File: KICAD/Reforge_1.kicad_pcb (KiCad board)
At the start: 2 copper layers, 57.9 x 76 mm, 94 parts, among them J1 USB_C_Receptacle_USB2.0_16P, J10 Conn_01x14_Pin, J11 Conn_01x12_Pin, J12 Conn_01x12_Pin, J14 Conn_01x12_Pin, J15 Conn_01x12_Pin, J3 Conn_01x02, J8 Conn_01x12_Pin, J9 Conn_01x14_Pin, Q1 SS8050, Q2 SS8050, SW1 SW_Push, SW2 SW_Push, U11 SN74LVC2G125DCUR, U2 CP2102N-Axx-xQFN28, U3 ICE40UP5K-SG48ITR, U4 AP2112K-1.2, U5 ESP32-WROOM-32D, U6 AMS1117-3.3, U8 W25Q32JVSS, Y1 SG-210STF

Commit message: Update schematic and PCB
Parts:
- removed C26, C27, C28: DNI, Capacitor_SMD:C_0805_2012Metric
- removed the G*** at (130.1, 58.2)
- removed R7, R8: 0R(5%), Resistor_SMD:R_0805_2012Metric_Pad1.20x1.40mm_HandSolder
- removed TP1, TP2, TP8: TestPoint, TestPoint:TestPoint_Pad_D1.0mm
- removed VBUS1: TestPoint, LED_SMD:LED_RGB_Wuerth-PLCC4_3.2x2.8mm_150141M173100
- added G***: LOGO, LOGO, F.Cu at (122.5, 87.4)
- added G***: LOGO, LOGO, B.Cu at (129.5, 60.2)
- added G***: LOGO, LOGO, B.Cu at (158.5, 66.4)
- C16, Q1, R10, R19, R4, R9, U2, U8: moved to F.Cu
- R20: footprint Resistor_SMD:R_0402_1005Metric -> Resistor_SMD:R_0805_2012Metric_Pad1.20x1.40mm_HandSolder
- SJ31, SJ34: moved to B.Cu
- moved C8 64.0 mm to (159.4, 60.4), turned to 0 degrees
- moved R1 62.3 mm to (117.0, 55.8)
- moved C9 61.5 mm to (159.4, 62.5), turned to 0 degrees
- moved SJ26 38.0 mm to (122.9, 107.0), turned to 0 degrees
- moved C16 37.9 mm to (128.7, 114.4), turned to -90 degrees
- moved C24 36.2 mm to (142.2, 108.3), turned to -90 degrees
- moved C2 33.9 mm to (116.9, 49.4), turned to 0 degrees
- moved SJ19 32.8 mm to (122.8, 99.5), turned to 0 degrees
- moved C1 31.1 mm to (116.8, 51.5), turned to 180 degrees
- moved C13 30.0 mm to (128.9, 99.2), turned to 90 degrees
- moved C14 29.6 mm to (138.4, 105.5)
- moved C12 29.0 mm to (126.8, 99.2), turned to 90 degrees
- moved SJ31 28.2 mm to (127.7, 99.3), turned to -90 degrees
- moved C5 27.9 mm to (131.6, 79.2), turned to -90 degrees
- moved C7 25.1 mm to (133.3, 84.6), turned to 180 degrees
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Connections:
- J10 pad 4: /TXD0 -> /RXD
- Q2 pad 2: /IO0 -> /~{DTR}
- Q2 pad 3: /~{DTR} -> /IO0
- U2 pad 26: /TXD -> /RXD0
- U5 pad 35: /TXD0 -> /RXD
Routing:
- net /VDD33: track 275.1 -> 0.00 mm, vias 12 -> 0
- net /EN: track 132.6 -> 0.00 mm, vias 2 -> 0
- net /VCCIO_2: track 72.4 -> 0.00 mm, vias 3 -> 0
- net /FT_SCK: track 67.6 -> 0.00 mm
- net /VCCIO_0: track 51.8 -> 0.00 mm, vias 6 -> 0
- net /CLK: track 48.1 -> 0.00 mm, vias 3 -> 0
- net /CDONE: track 43.8 -> 0.00 mm, vias 3 -> 0
- net /FT_SSn: track 43.0 -> 0.00 mm, vias 5 -> 0
- net /+1.2V_CORE: track 42.3 -> 0.00 mm
- net /USB_DP: track 41.2 -> 0.00 mm, vias 4 -> 0
- net /IOB_25B_G3: track 41.1 -> 0.00 mm, vias 2 -> 0
- net /EXT_5V: track 39.4 -> 0.00 mm
- net /IO0: track 36.2 -> 0.00 mm, vias 4 -> 0
- net /FPGA_SO: track 33.8 -> 0.00 mm
- net /FPGA_SI: track 31.8 -> 0.00 mm, vias 2 -> 0
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- added copper zone on F.Cu, net /VDD33
- removed copper zone on F.Cu, net GND
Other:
- board size 57.9 x 76 mm -> 66.5 x 80.4 mm
- board text added: "AMRIT"
- board text added: "SURAJ"

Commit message: UPDATED PCB
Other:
- board text added: "BOOT"
- board text added: "EN"
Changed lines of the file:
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@@
 		(tags "resistor handsolder")
 		(property "Reference" "R9"
-			(at -0.06 -1.71 90)
+			(at -1.85 -1.71 180)
 			(layer "F.SilkS")
 			(effects
 				(font
-					(size 1 1)
-					(thickness 0.15)
+					(size 0.5 0.5)
+					(thickness 0.125)
 				)
 			)
@@
 			(effects
 				(font
-					(size 1 1)
-					(thickness 0.15)
+					(size 0.5 0.5)
+					(thickness 0.125)
 				)
 			)
@@
 		(tags "SOT TO_SOT_SMD")
 		(property "Reference" "Q1"
-			(at 0.14 2.37 0)
+			(at 0.14 2.65 0)
 			(layer "F.SilkS")
 			(effects
 				(font
-					(size 1 1)
-					(thickness 0.15)
+					(size 0.5 0.5)
+					(thickness 0.125)
 				)
 			)
@@
 			(effects
 				(font
-					(size 1 1)
-					(thickness 0.15)
+					(size 0.5 0.5)
+					(thickness 0.125)
 				)
 			)
@@
 		(tags "resistor handsolder")
 		(property "Reference" "R10"
-			(at 0.05 1.65 90)
+			(at -1.8 2.1 180)
 			(layer "F.SilkS")
 			(effects
 				(font
-					(size 1 1)
-					(thickness 0.15)
+					(size 0.5 0.5)
+					(thickness 0.125)
 				)
 			)
@@
 		(tags "resistor handsolder")
 		(property "Reference" "R26"
-			(at 0 -1.65 90)
+			(at 0 -1.825 180)
 			(layer "F.SilkS")
 			(effects
 				(font
-					(size 1 1)
-					(thickness 0.15)
+					(size 0.5 0.5)
+					(thickness 0.125)
 				)
 			)
@@
 		(tags "capacitor")
 		(property "Reference" "C10"
-			(at 0 -1.68 90)
+			(at -0.075 -1.925 180)
 			(layer "F.SilkS")
 			(effects
 				(font
-					(size 1 1)
-					(thickness 0.15)
+					(size 0.5 0.5)
+					(thickness 0.125)
 				)
 			)
@@
 		(layer "Edge.Cuts")
 	)
+	(gr_text "EN"
+		(at 119.125 63.825 0)
+		(layer "F.SilkS")
+		(effects
+			(font
+				(size 0.5 0.5)
+				(thickness 0.1)
+				(bold yes)
+			)
+			(justify left bottom)
+		)
+	)
+	(gr_text "BOOT\n"
+		(at 157.525 83.575 0)
+		(layer "F.SilkS")
+		(effects
+			(font
+				(size 0.5 0.5)
+				(thickness 0.125)
+				(bold yes)
+			)
+			(justify left bottom)
+		)
+	)
 	(gr_text "SURAJ"

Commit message: UPDATED PCB
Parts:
- moved G*** 50.0 mm to (167.7, 108.7), turned to 90 degrees
- moved C10 2.12 mm to (163.6, 81.6), turned to 0 degrees
- moved J15 1.09 mm to (159.7, 94.9)
- moved R26 0.97 mm to (163.5, 79.0), turned to 0 degrees
- moved C24 0.88 mm to (142.1, 109.2)
- moved J8 0.85 mm to (111.5, 95.1)
- moved R14 0.43 mm to (144.2, 108.9)
- moved R2 0.29 mm to (145.3, 76.5)
- moved C4 0.14 mm to (143.2, 76.4)
- moved U8 0.05 mm to (148.3, 103.7)
- renumbered PWR_LED1 to PWR_LED
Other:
- board size 66.5 x 80.4 mm -> 64.8 x 80.2 mm

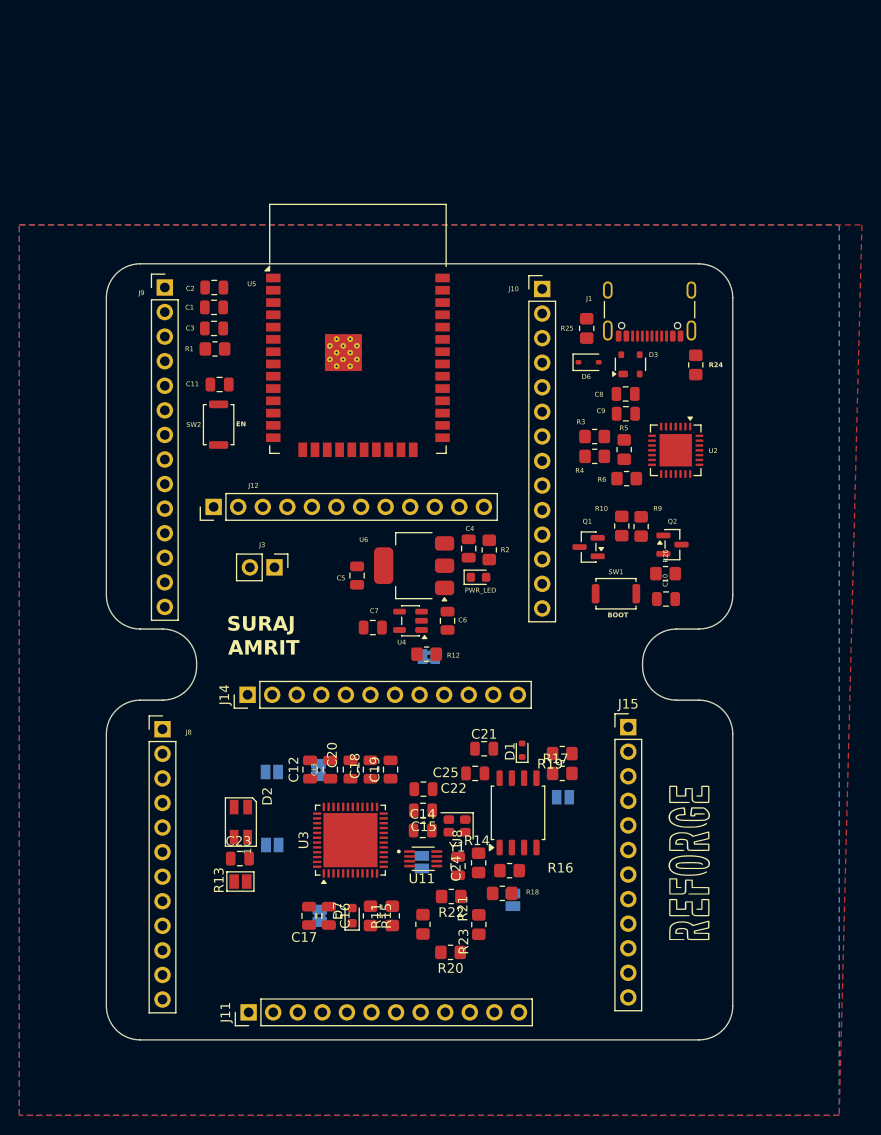
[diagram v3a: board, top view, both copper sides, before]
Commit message: Added some more diodes and Placement done
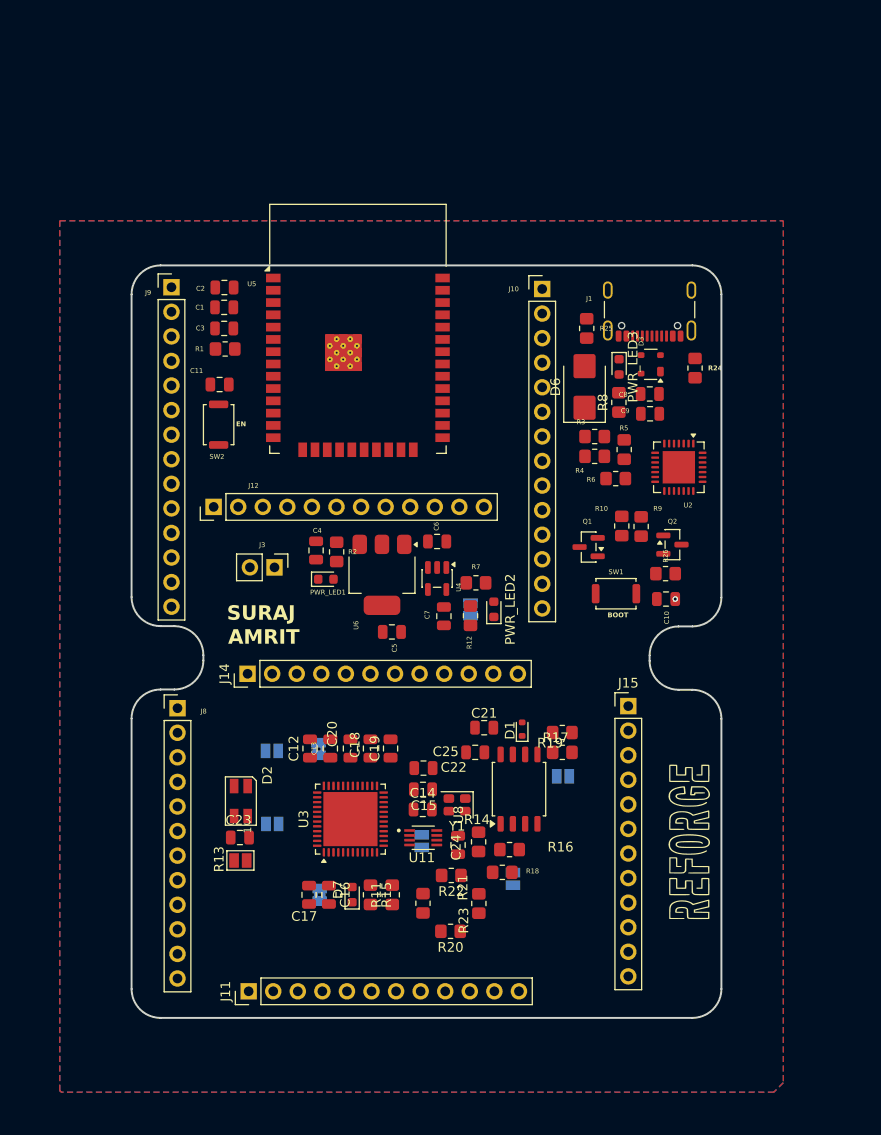
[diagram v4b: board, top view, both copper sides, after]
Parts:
- added G***: LOGO, LOGO, B.Cu at (135.1, 97.1)
- added PWR_LED2: RED LED, LED_SMD:LED_0603_1608Metric, F.Cu at (145.8, 82.7)
- added PWR_LED3: RED LED, LED_SMD:LED_0603_1608Metric, F.Cu at (158.7, 57.6)
- added R7: 330R, Resistor_SMD:R_0805_2012Metric_Pad1.20x1.40mm_HandSolder, F.Cu at (143.9, 80.0)
- added R8: 1K, Resistor_SMD:R_0805_2012Metric_Pad1.20x1.40mm_HandSolder, F.Cu at (158.7, 61.3)
- D6: footprint Diode_SMD:D_SOD-323 -> Diode_SMD:D_SMB
- R2: value 2K(5%) -> 330R
- moved C4 15.8 mm to (127.4, 76.6)
- moved PWR_LED1 15.8 mm to (128.4, 79.6)
- moved R2 15.8 mm to (129.5, 76.8)
- moved C6 8.27 mm to (139.9, 75.7), turned to 180 degrees
- moved C7 7.44 mm to (140.6, 83.4), turned to -90 degrees
- moved C5 6.85 mm to (135.2, 85.0), turned to 0 degrees
- moved SJ34 6.50 mm to (143.4, 82.7), turned to -90 degrees
- moved R12 6.03 mm to (143.4, 83.3), turned to -90 degrees
- moved U4 5.17 mm to (139.9, 79.5), turned to -90 degrees
- moved U6 3.46 mm to (134.2, 79.1), turned to -90 degrees
- moved J8 2.67 mm to (113.1, 92.9)
- moved D6 2.59 mm to (155.2, 59.7), turned to 90 degrees
- moved C8 2.50 mm to (161.9, 60.4)
- moved C9 2.50 mm to (161.9, 62.5)
- moved U8 2.45 mm to (148.4, 101.3)
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- renumbered PWR_LED to PWR_LED1
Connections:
- J15 pad 10: /FT_SCK -> /CLK
- J15 pad 11: /FPGA_SO -> /MISO
- J15 pad 8: /FPGA_SI -> /MOSI
- J15 pad 9: /FT_SSn -> /CS
- R16 pad 2: /FT_SSn -> /CS
- R17 pad 2: /FT_SCK -> /SCK
- R2 pad 1: /EXT_5V -> /VDD33
- R20 pad 1: /FPGA_SO -> /MISO
- R21 pad 2: /FPGA_SO -> /MISO
- R22 pad 2: /FPGA_SI -> /MOSI
- R23 pad 2: /FPGA_SI -> /MOSI
- U3 pad 14: /FPGA_SO -> /MISO
- U3 pad 15: /FT_SCK -> /SCK
- U3 pad 16: /FT_SSn -> /CS
- U3 pad 17: /FPGA_SI -> /MOSI
- U8 pad 1: /FT_SSn -> /CS
- U8 pad 6: /FT_SCK -> /SCK
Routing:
- net GND: vias 0 -> 1
- added copper zone on F.Cu, net GND
- removed copper zone on F.Cu, net /VDD33
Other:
- board size 64.8 x 80.2 mm -> 61 x 77.8 mm

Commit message: Did Routing and updates schematic
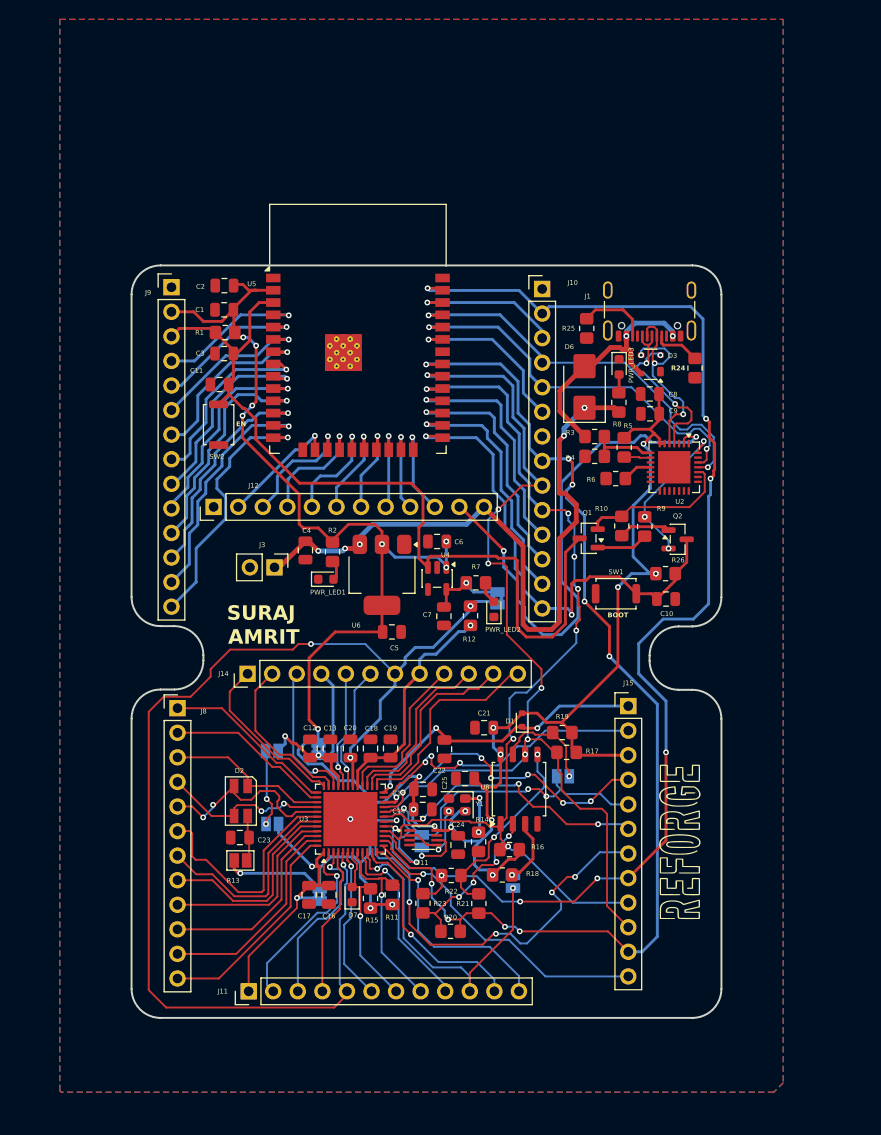
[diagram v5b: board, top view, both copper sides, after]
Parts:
- R8: value 1K -> 330R
- moved SJ34 3.02 mm to (146.2, 81.5)
- moved C22 2.92 mm to (140.7, 97.2), turned to -90 degrees
- moved C25 2.90 mm to (142.8, 100.2)
- moved C3 2.60 mm to (117.9, 56.2)
- moved R1 1.70 mm to (118.0, 54.1)
- moved C4 1.10 mm to (126.3, 76.6)
- moved G*** 0.97 mm to (166.7, 106.5)
- moved D1 0.95 mm to (148.7, 94.1)
- moved Q1 0.90 mm to (155.6, 75.3)
- moved Q2 0.77 mm to (164.8, 75.5)
- moved U2 0.47 mm to (164.4, 68.0)
- moved R17 0.45 mm to (153.3, 97.5)
- moved R2 0.43 mm to (129.1, 76.8)
- moved R15 0.38 mm to (133.0, 112.6)
- moved R9 0.38 mm to (161.4, 74.1)
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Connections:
- J15 pad 10: /CLK -> /SCK
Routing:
- net /VDD33: track 0.00 -> 250.6 mm, vias 0 -> 24
- net /MOSI: track 0.00 -> 132.9 mm, vias 0 -> 8
- net /+1.2V_CORE: track 0.00 -> 124.2 mm, vias 0 -> 4
- net /MISO: track 0.00 -> 115.6 mm, vias 0 -> 9
- net /SCK: track 0.00 -> 111.9 mm, vias 0 -> 7
- net /CS: track 0.00 -> 96.4 mm, vias 0 -> 7
- net /EN: track 0.00 -> 88.4 mm
- net /EXT_5V: track 0.00 -> 72.4 mm, vias 0 -> 5
- net /CLK: track 0.00 -> 54.3 mm, vias 0 -> 2
- net /IO0: track 0.00 -> 51.7 mm, vias 0 -> 2
- net /IOB_31B: track 0.00 -> 47.1 mm, vias 0 -> 5
- net /RXD: track 0.00 -> 42.1 mm, vias 0 -> 2
- net /RXD0: track 0.00 -> 39.9 mm, vias 0 -> 2
- net /IOB_18A: track 0.00 -> 34.7 mm, vias 0 -> 2
- net /IOB_25B_G3: track 0.00 -> 33.2 mm, vias 0 -> 3
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
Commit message: updated pcb
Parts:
- removed the G*** at (158.5, 66.4)
- removed the G*** at (135.1, 97.1)
- added G***: LOGO, LOGO, B.Cu at (158.4, 67.4)
- added G***: LOGO, LOGO, B.Cu at (138.1, 115.0)
- moved C24 0.15 mm to (142.2, 107.0)
- moved R14 0.11 mm to (144.3, 106.8)
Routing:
- net /VDD33: track 250.6 -> 308.9 mm, vias 24 -> 27
- net GND: track 0.00 -> 21.5 mm, vias 1 -> 14
- net /SCK: track 111.9 -> 117.1 mm
- net Net-(U8-~{HOLD}/~{RESET}/IO_{3}): track 11.1 -> 13.5 mm
- net /EXT_5V: track 72.4 -> 74.6 mm, vias 5 -> 4
- net /+1.2V_CORE: track 124.2 -> 126.1 mm
- net Net-(U8-~{WP}/IO_{2}): track 6.95 -> 8.18 mm
- net /IOB_29B: track 29.7 -> 30.8 mm
- net Net-(Y1-~{ST}): track 5.10 -> 6.17 mm
- net /CLK: track 54.3 -> 55.2 mm
- net /~{DTR}: track 16.2 -> 17.0 mm
- net /IOB_24A: track 31.7 -> 32.6 mm
- net /CS: track 96.4 -> 95.7 mm, vias 7 -> 6
- net /VDD12: track 8.00 -> 8.63 mm
- net /IOB_18A: track 34.7 -> 35.3 mm
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
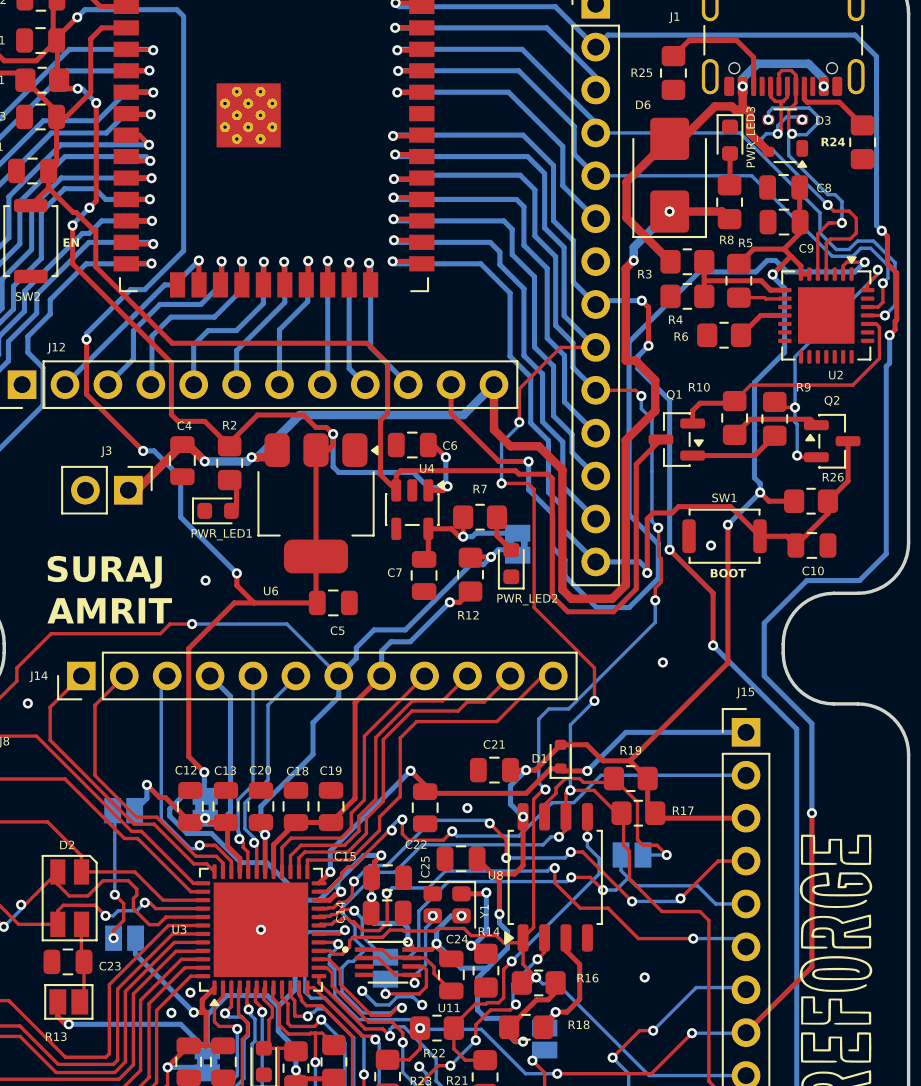
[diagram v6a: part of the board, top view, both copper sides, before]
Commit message: Updated a VIA
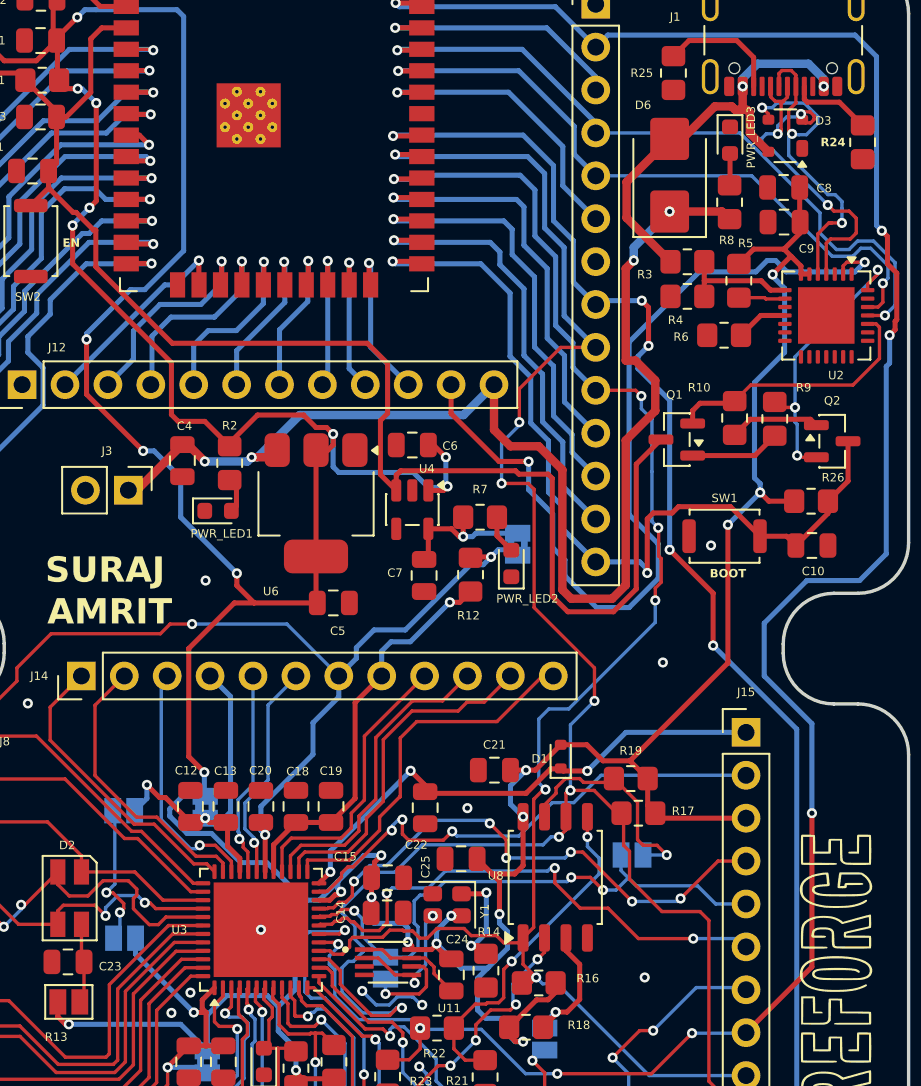
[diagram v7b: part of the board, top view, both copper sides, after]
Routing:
- net /USB_DP: track 20.4 -> 22.4 mm
- net /USB_DN: track 22.7 -> 23.7 mm
- net /IOB_25B_G3: track 33.2 -> 33.9 mm
- net /VIO_BANK_0_2: track 8.07 -> 8.70 mm
- net /LED_B: track 17.6 -> 18.2 mm
